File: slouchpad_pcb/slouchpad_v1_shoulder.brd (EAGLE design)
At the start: 36 x 15 mm, 3 parts

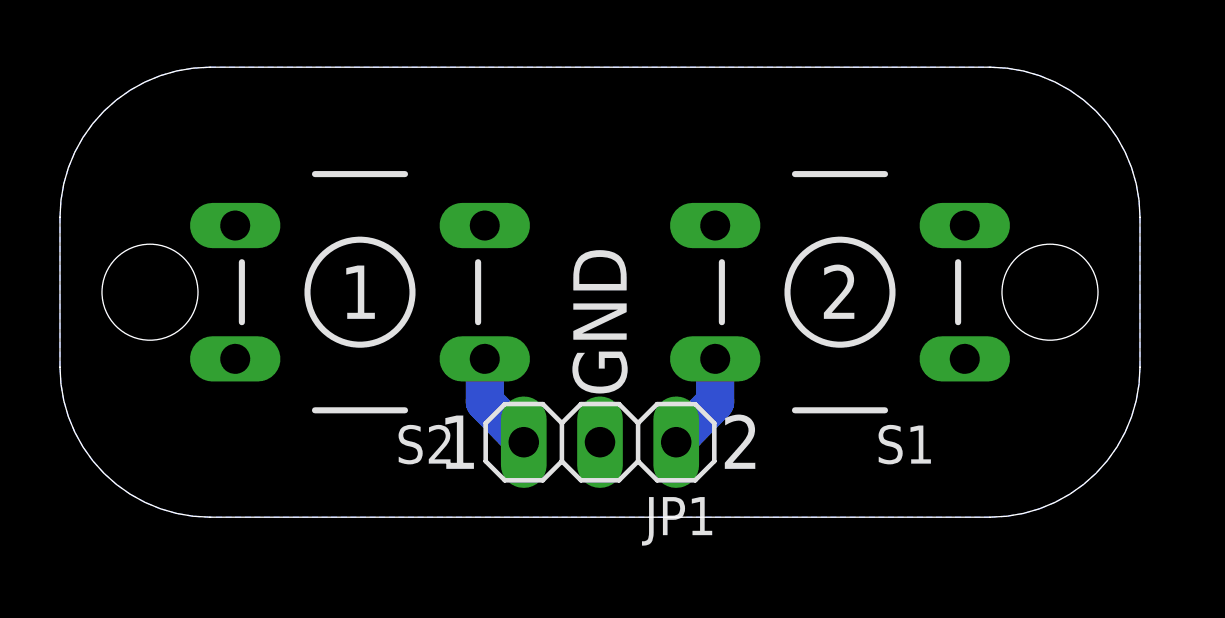
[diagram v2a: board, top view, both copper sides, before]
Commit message: Added dimensions to baord drawings and fixed button 5 position to have correct spacing.
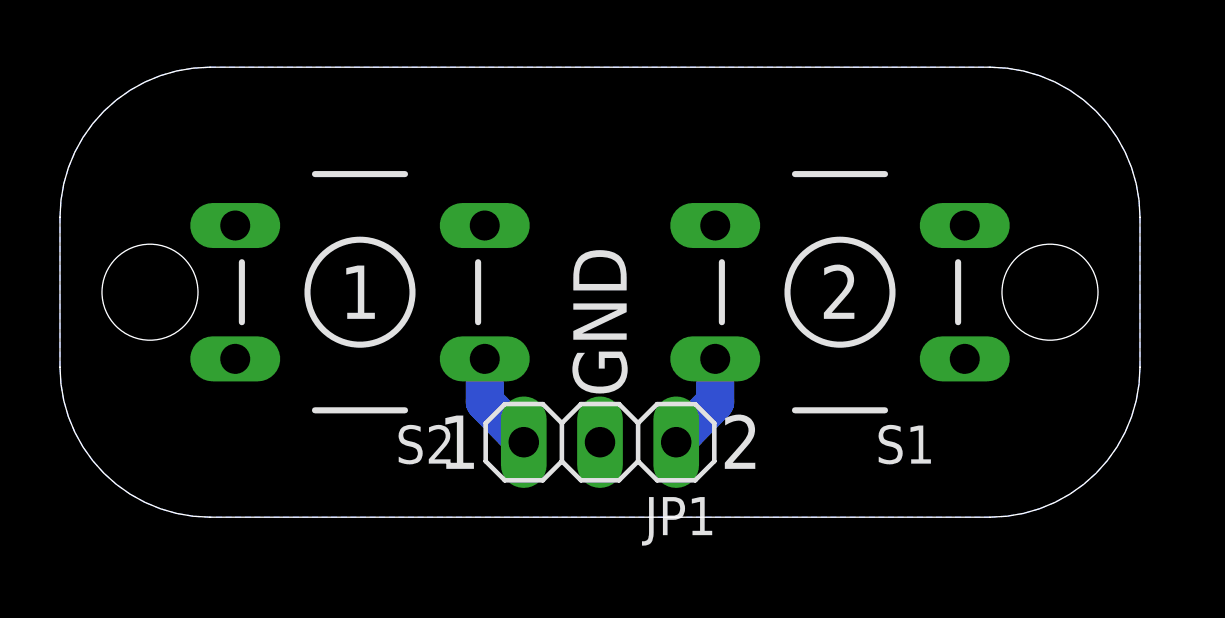
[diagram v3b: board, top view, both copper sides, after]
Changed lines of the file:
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@@
 <setting verticaltext="up"/>
 </settings>
-<grid distance="0.5" unitdist="mm" unit="mm" style="lines" multiple="1" display="yes" altdistance="0.025" altunitdist="inch" altunit="inch"/>
+<grid distance="0.25" unitdist="mm" unit="mm" style="lines" multiple="1" display="yes" altdistance="0.125" altunitdist="mm" altunit="mm"/>
 <layers>
 <layer number="1" name="Top" color="4" fill="1" visible="yes" active="yes"/>
@@
 <layer number="21" name="tPlace" color="7" fill="1" visible="yes" active="yes"/>
 <layer number="22" name="bPlace" color="7" fill="1" visible="no" active="yes"/>
-<layer number="23" name="tOrigins" color="15" fill="1" visible="no" active="yes"/>
+<layer number="23" name="tOrigins" color="15" fill="1" visible="yes" active="yes"/>
 <layer number="24" name="bOrigins" color="15" fill="1" visible="no" active="yes"/>
 <layer number="25" name="tNames" color="7" fill="1" visible="no" active="yes"/>
@@
 <layer number="45" name="Holes" color="7" fill="1" visible="yes" active="yes"/>
 <layer number="46" name="Milling" color="3" fill="1" visible="no" active="yes"/>
-<layer number="47" name="Measures" color="7" fill="1" visible="no" active="yes"/>
+<layer number="47" name="Measures" color="7" fill="1" visible="yes" active="yes"/>
 <layer number="48" name="Document" color="7" fill="1" visible="yes" active="yes"/>
 <layer number="49" name="Reference" color="7" fill="1" visible="yes" active="yes"/>
@@
 <text x="14" y="2.5" size="1.778" layer="100" rot="R180" align="center-left">1</text>
 <text x="22" y="2.5" size="1.778" layer="100" align="center-left">2</text>
+<dimension x1="10" y1="7.5" x2="26" y2="7.5" x3="18" y3="17.625" textsize="1.778" layer="47" dtype="horizontal"/>
+<dimension x1="0" y1="10" x2="10" y2="7.5" x3="5" y3="17.625" textsize="1.778" layer="47" dtype="horizontal"/>
+<dimension x1="26" y1="7.5" x2="36" y2="10" x3="31" y3="17.625" textsize="1.778" layer="47" dtype="horizontal"/>
+<dimension x1="0" y1="5" x2="3" y2="7.5" x3="1.5" y3="-3.75" textsize="1.778" layer="47" dtype="horizontal"/>
+<dimension x1="33" y1="7.5" x2="36" y2="5" x3="34.5" y3="-3.75" textsize="1.778" layer="47" dtype="horizontal"/>
+<dimension x1="3" y1="7.5" x2="33" y2="7.5" x3="18" y3="-3.75" textsize="1.778" layer="47" dtype="horizontal"/>
+<wire x1="-1" y1="7.5" x2="37" y2="7.5" width="0.125" layer="47" style="longdash"/>
+<dimension x1="-1" y1="7.5" x2="5" y2="0" x3="-1.25" y3="3.75" textsize="1.778" layer="47" dtype="vertical"/>
+<dimension x1="5" y1="15" x2="5" y2="0" x3="-5.25" y3="7.5" textsize="1.778" layer="47" dtype="vertical"/>
+<dimension x1="0" y1="10" x2="36" y2="10" x3="18" y3="22.25" textsize="1.778" layer="47"/>
+<dimension x1="33" y1="9.1" x2="33" y2="5.9" x3="39.25" y3="7.5" textsize="1.778" layer="47" dtype="diameter"/>
+<dimension x1="5" y1="10" x2="0.97174375" y2="12.961953125" x3="-5.312334375" y3="17.582596875" textsize="1.778" layer="47" dtype="radius"/>
 </plain>
 <attributes>
@@
 </class>
 </classes>
-<designrules name="default *">
+<designrules name="oshpark-2layer">
 <description language="de">&lt;b&gt;EAGLE Design Rules&lt;/b&gt;
 &lt;p&gt;
@@
 Einstellungen hier und speichern die Design Rules unter
 einem neuen Namen ab.</description>
-<description language="en">&lt;b&gt;EAGLE Design Rules&lt;/b&gt;
+<description language="en">&lt;b&gt;Laen's PCB Order Design Rules&lt;/b&gt;
 &lt;p&gt;
-The default Design Rules have been set to cover
-a wide range of applications. Your particular design
-may have different requirements, so please make the
-necessary adjustments and save your customized
-design rules under a new name.</description>
+Please make sure your boards conform to these design rules.</description>
 <param name="layerSetup" value="(1*16)"/>
-<param name="mtCopper" value="0.035mm 0.035mm 0.035mm 0.035mm 0.035mm 0.035mm 0.035mm 0.035mm 0.035mm 0.035mm 0.035mm 0.035mm 0.035mm 0.035mm 0.035mm 0.035mm"/>
-<param name="mtIsolate" value="1.5mm 0.15mm 0.2mm 0.15mm 0.2mm 0.15mm 0.2mm 0.15mm 0.2mm 0.15mm 0.2mm 0.15mm 0.2mm 0.15mm 0.2mm"/>
-<param name="mdWireWire" value="20mil"/>
-<param name="mdWirePad" value="20mil"/>
-<param name="mdWireVia" value="20mil"/>
-<param name="mdPadPad" value="20mil"/>
-<param name="mdPadVia" value="20mil"/>
-<param name="mdViaVia" value="20mil"/>
-<param name="mdSmdPad" value="8mil"/>
-<param name="mdSmdVia" value="8mil"/>
-<param name="mdSmdSmd" value="8mil"/>
+<param name="mtCopper" value="0.0356mm 0.0356mm 0.0356mm 0.0356mm 0.0356mm 0.0356mm 0.0356mm 0.0356mm 0.0356mm 0.0356mm 0.0356mm 0.0356mm 0.0356mm 0.0356mm 0.0356mm 0.0356mm"/>
+<param name="mtIsolate" value="1.5011mm 0.1499mm 0.2007mm 0.1499mm 0.2007mm 0.1499mm 0.2007mm 0.1499mm 0.2007mm 0.1499mm 0.2007mm 0.1499mm 0.2007mm 0.1499mm 0.2007mm"/>
+<param name="mdWireWire" value="6mil"/>
+<param name="mdWirePad" value="6mil"/>
+<param name="mdWireVia" value="6mil"/>
+<param name="mdPadPad" value="6mil"/>
+<param name="mdPadVia" value="6mil"/>
+<param name="mdViaVia" value="6mil"/>
+<param name="mdSmdPad" value="6mil"/>
+<param name="mdSmdVia" value="6mil"/>
+<param name="mdSmdSmd" value="6mil"/>
 <param name="mdViaViaSameLayer" value="8mil"/>
 <param name="mnLayersViaInSmd" value="2"/>
-<param name="mdCopperDimension" value="20mil"/>
-<param name="mdDrill" value="8mil"/>
+<param name="mdCopperDimension" value="15mil"/>
+<param name="mdDrill" value="6mil"/>
 <param name="mdSmdStop" value="0mil"/>
-<param name="msWidth" value="10mil"/>
-<param name="msDrill" value="24mil"/>
-<param name="msMicroVia" value="9.99mm"/>
+<param name="msWidth" value="6mil"/>
+<param name="msDrill" value="13mil"/>
+<param name="msMicroVia" value="13mil"/>
 <param name="msBlindViaRatio" value="0.5"/>
 <param name="rvPadTop" value="0.25"/>
@@
 <param name="rvMicroViaOuter" value="0.25"/>
 <param name="rvMicroViaInner" value="0.25"/>
-<param name="rlMinPadTop" value="10mil"/>
+<param name="rlMinPadTop" value="7mil"/>
 <param name="rlMaxPadTop" value="20mil"/>
-<param name="rlMinPadInner" value="10mil"/>
+<param name="rlMinPadInner" value="7mil"/>
 <param name="rlMaxPadInner" value="20mil"/>
-<param name="rlMinPadBottom" value="10mil"/>
+<param name="rlMinPadBottom" value="7mil"/>
 <param name="rlMaxPadBottom" value="20mil"/>
-<param name="rlMinViaOuter" value="8mil"/>
+<param name="rlMinViaOuter" value="7mil"/>
 <param name="rlMaxViaOuter" value="20mil"/>
-<param name="rlMinViaInner" value="8mil"/>
+<param name="rlMinViaInner" value="7mil"/>
 <param name="rlMaxViaInner" value="20mil"/>
 <param name="rlMinMicroViaOuter" value="4mil"/>
@@
 <param name="mvStopFrame" value="1"/>
 <param name="mvCreamFrame" value="0"/>
-<param name="mlMinStopFrame" value="4mil"/>
-<param name="mlMaxStopFrame" value="4mil"/>
+<param name="mlMinStopFrame" value="2.5mil"/>
+<param name="mlMaxStopFrame" value="2.5mil"/>
 <param name="mlMinCreamFrame" value="0mil"/>
 <param name="mlMaxCreamFrame" value="0mil"/>
@@
 <param name="srMinRoundness" value="0mil"/>
 <param name="srMaxRoundness" value="0mil"/>
-<param name="slThermalIsolate" value="0mil"/>
+<param name="slThermalIsolate" value="10mil"/>
 <param name="slThermalsForVias" value="0"/>
 <param name="dpMaxLengthDifference" value="10mm"/>
